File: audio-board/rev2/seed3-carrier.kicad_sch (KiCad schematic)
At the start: 55 parts, among them J1 AudioJack2_Switch, J2 AudioJack2, J3 POWER_BOARD, J4 DISPLAY_UART, J5 SJ3-35063AG, J8 LINE_OUT, J9 SJ3-35063AG, Q1 AO3401A, Q4 2N7002, U1 TLV9062IDR, U2 TPA6132A2RTE, U4 TXU0101

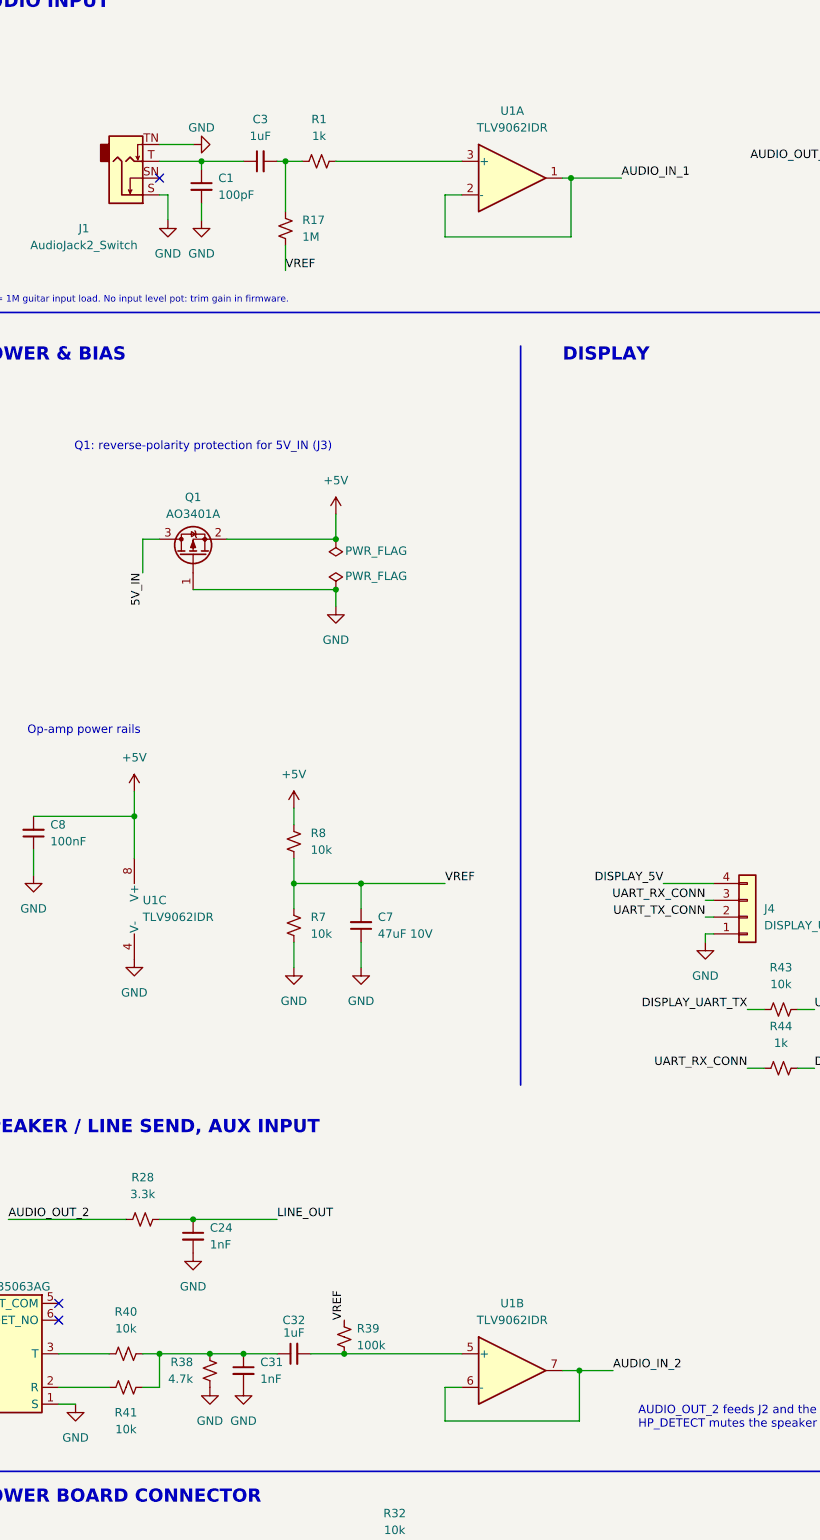
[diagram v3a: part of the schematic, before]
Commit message: Feed the AUX input straight to the Daisy and use a single op-amp
The Seed3's inputs are AC-coupled and the TAC5242 presents about 5k,
so the R40/R41 sum can drive Daisy pin 17 directly. This drops U1B,
C32 and R39, and R38 becomes a 100k DC return. U1 is now a TLV9061 in
SOT-23-5, with a two-unit project symbol, re-placed at the end of the
guitar row with C8 beside its V+ pin. TEST_PLAN 5.17 checks the AUX
level with the Daisy fitted.

Co-Authored-By: Claude Opus 5.5 <noreply@anthropic.com>
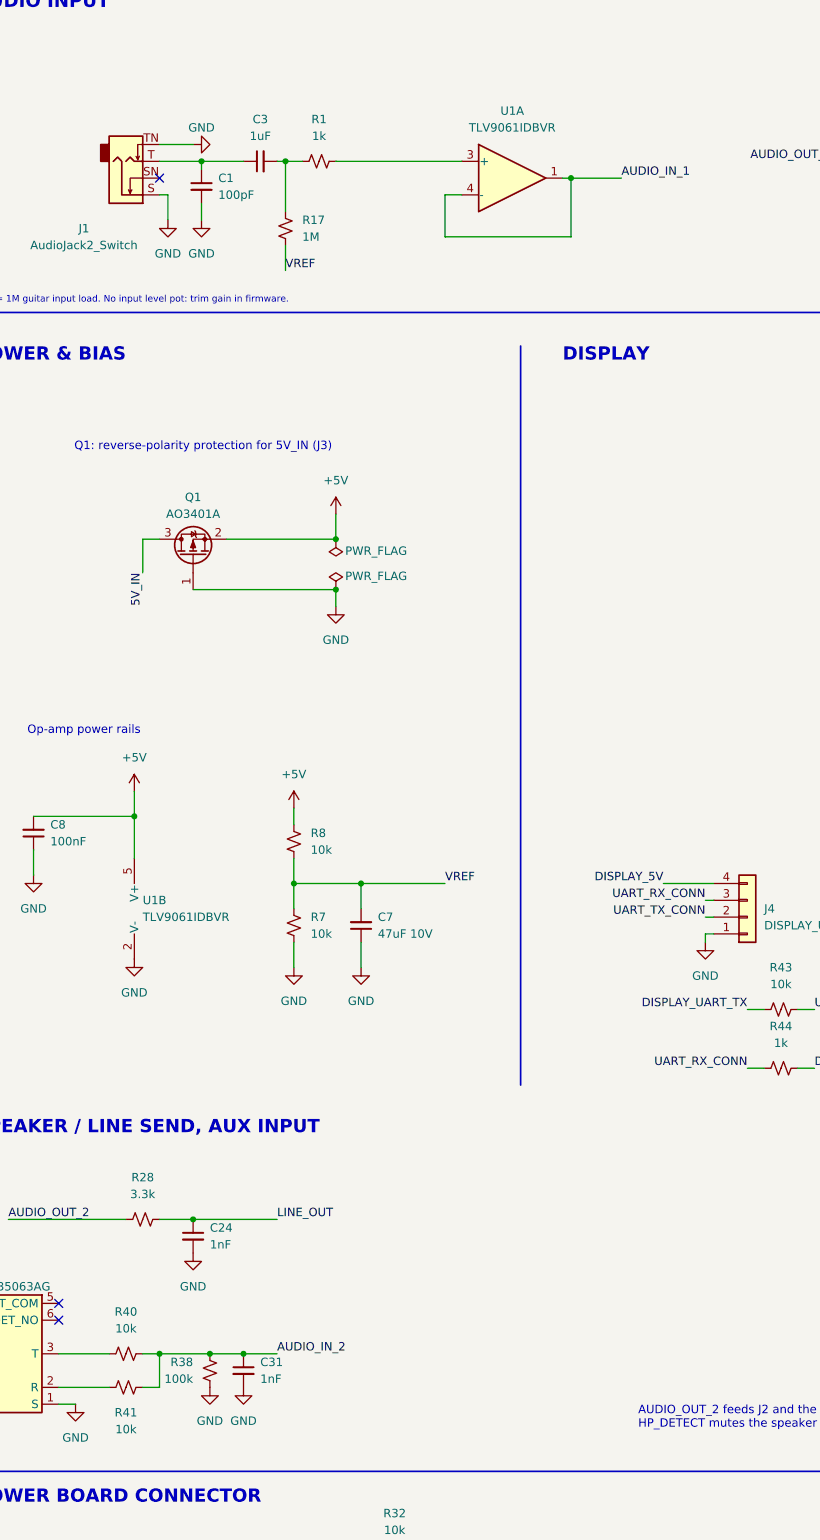
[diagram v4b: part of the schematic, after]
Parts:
- removed C32: 1uF, Capacitor_SMD:C_1206_3216Metric_Pad1.33x1.80mm_HandSolder, symbol Device:C_Small
- removed R39: 100k, Resistor_SMD:R_1206_3216Metric_Pad1.30x1.75mm_HandSolder, symbol Device:R_Small_US
- removed unit 2 of U1
- R38: value 4.7k -> 100k; LCSC C17936 -> C17900
- U1: value TLV9062IDR -> TLV9061IDBVR; footprint Package_SO:SOIC-8_3.9x4.9mm_P1.27mm -> Package_TO_SOT_SMD:SOT-23-5; symbol Amplifier_Operational:TL072 -> seed3-carrier:TLV9061DBV; LCSC C398355 -> C398358
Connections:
- net +5V: now also U1.5 (V+); no longer U1.8 (V+)
- net AUDIO_IN_1: now also U1.4 (-); no longer U1.2 (-)
- net AUDIO_IN_2: now also C31.1, R38.1, R40.2, R41.2
- net GND: now also U1.2 (V-); no longer U1.4 (V-)

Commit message: Remove U4, C37, C38 and R26 and tie U2 EN to +5V
The codec already powers down its DAC when an IWDG reset stops its
clocks, which silences the headphones as well as J2. Driving U2's EN
from the Daisy needed a level translator because the Daisy can run
from USB with +5V off, so drop it and leave U2 always on.

Co-Authored-By: Claude Opus 5.5 <noreply@anthropic.com>
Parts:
- removed C37, C38: 100nF, Capacitor_SMD:C_1206_3216Metric_Pad1.33x1.80mm_HandSolder, symbol Device:C_Small
- removed R26: 100k, Resistor_SMD:R_1206_3216Metric_Pad1.30x1.75mm_HandSolder, symbol Device:R_Small_US
- removed U4: TXU0101, Package_TO_SOT_SMD:SOT-23-6, symbol seed3-carrier:TXU0101DBV
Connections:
- net U2_EN is gone; now on net +5V: U2.13 (EN)
- net 3V3_D: no longer names the net of A1.38 (3V3_D)
- net HP_EN: no longer names the net of A1.33 (SAI2_SD_A)
- no-connect marks 27 -> 29
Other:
- note added: "U2 EN is tied to +5V: the headphone amp is on whenever +5V is up. A hung Daisy is muted by the codec, not by U2. The firmware feeds the STM32 internal watchdog (IWDG) only from the audio callback: if audio stops, the STM32 resets, its clocks stop, and the TAC5242 powers down its DAC (both outputs). Its pins float, and R37 holds SPK_EN low (Q4 off, speaker amp muted). The speaker amp mute is SPK_M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"
- note added: "U2: TPA6132A2 DirectPath, gain 0 dB (G0 high, G1 low). Outputs sit at 0 V: no output caps. C12/C13 with the 19.8k internal input R: 1.7 Hz high-pass. EN tied to +5V (always on). Layout: run SGND straight to the J5 sleeve pin. HPVDD/HPVSS are made inside U2: caps only."
- note removed: "HP_EN (Daisy pin 33) drives U2 EN through U4 (TXU0101, 3V3_D to +5V). U4 has a pull-down on A and goes Hi-Z when either supply is off, and R26 holds U2_EN low, so U2 stays off while the Daisy is absent, booting, in DFU, being reset, or running from USB with +5V off. The firmware feeds the STM32 internal watchdog (IWDG) only from the audio callback: if audio stops, the STM32 resets, its pins float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"
- note removed: "U2: TPA6132A2 DirectPath, gain 0 dB (G0 high, G1 low). Outputs sit at 0 V: no output caps. C12/C13 with the 19.8k internal input R: 1.7 Hz high-pass. EN = U2_EN from U4, pulled low by R26. Layout: run SGND straight to the J5 sleeve pin. HPVDD/HPVSS are made inside U2: caps only."

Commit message: Add a +5V sense on Daisy pin 22 to keep USB-only audio out of U2
With the Daisy on USB and +5V off, U2's charge pump rails sit at 0 V,
so its inputs are rated only to about +-0.3 V, while C12/C13 pass pin
18's full-scale +-1.4 V. R45/R46 (100k/100k) put +5V/2 on 5V_SENSE
(ADC_0) so the firmware can hold the outputs silent while +5V is down.

DESIGN.md sets the firmware thresholds and settle time and notes the
fast-power-loss limit; TEST_PLAN 5.18 scopes the transitions.

Co-Authored-By: Claude Opus 5.5 <noreply@anthropic.com>
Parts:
- added R45, R46: 100k, Resistor_SMD:R_1206_3216Metric_Pad1.30x1.75mm_HandSolder, symbol Device:R_Small_US
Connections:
- net +5V: now also R45.1
- net GND: now also R46.2
- net 5V_SENSE: now reaches A1.22 (ADC_0)
- net 5V_SENSE: now also R45.2, R46.1
- no-connect marks 29 -> 28

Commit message: Re-lay out the carrier schematic into framed functional sections
Group the sheet into eleven dashed, titled sections laid out left to
right (inputs and supply, Daisy and display, outputs, power board and
mute), moving each block rigidly so no connection changes. Misplaced
parts move to their own blocks: the AUX input, C17/C18, FB1/C30, J2/J8.

Rewrite every note in one style inside its section, correct the stale
HP_DETECT/SPK_EN note, and add notes for the AUX input, VREF, display
resistors and Daisy sockets. Update the title block, set J1/J2 to
NRJ4HF and C7/C18 to the 16 V parts on the BOM (board values match).

Co-Authored-By: Claude Opus 5.5 <noreply@anthropic.com>
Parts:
- C18, C7: value 47uF 10V -> 47uF 16V
- J1: value AudioJack2_Switch -> NRJ4HF
- J2: value AudioJack2 -> NRJ4HF
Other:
- note added: "A1 plugs into two 1×20 sockets. Unused pins are no-connect. USB stays on the module."
- note added: "AUDIO_OUT_2 drives J2 (external) and J8 (speaker amp) directly. R28/C24: ≈ 48 kHz low-pass. R4: DC return. With headphones in, the firmware drives SPK_EN low. J2 stays live."
- note added: "AUX INPUT"
- note added: "DAISY SEED3"
- note added: "GUITAR INPUT"
- note added: "HEADPHONE AMPLIFIER"
- note added: "HEADPHONE JACK & DETECT"
- note added: "J3 goes to the power board (JST-XH, 8 pins). Pins 5–7 are 3.3 V logic: nothing above 3.3 V on them. SPK_MUTE is open drain. The power board pulls it up, so the speaker amp stays muted unless SPK_EN is high. R32, R35 and R33 limit current into an unpowered Daisy. R34 holds PWR_HOLD low while the Daisy is absent or booting."
- note added: "J5 pins 5–6: isolated N/O switch, closes on plug insertion. HP_DETECT is LOW with headphones in. No external pull-up: the firmware enables PG9's internal pull-up. Bring-up: short TP11 to GND to simulate a plug."
- note added: "LINE OUT & SPEAKER SEND"
- note added: "MID-RAIL REFERENCE & OP-AMP SUPPLY"
- note added: "Mono to both channels, 16–64 Ω headphones. R2/C2: ≈ 64 kHz low-pass for DAC noise. U2: TPA6132A2 DirectPath, 0 dB inverting (G0 high, G1 low). Outputs sit at 0 V: no output caps. C12/C13 with U2's 19.8 kΩ inputs: 1.7 Hz high-pass. EN tied to +5V: always on. Layout: run SGND straight to the J5 sleeve. HPVDD/HPVSS are made inside U2: caps only."
- note added: "OUTPUT MUTE & +5V SENSE"
- note added: "POWER INPUT"
- note added: "Passive stereo-to-mono sum straight into AUDIO_IN_2. The Seed3 input is AC-coupled (≈ 5 kΩ): no buffer or coupling cap needed. R38 is the source's DC return. C31: RF filter (≈ 65 kHz)."
- note added: "Q1: reverse-polarity protection for 5V_IN (J3). C18 (low-ESR) damps the harness ringing. C17 is the entry ceramic."
- note added: "R17 (1 MΩ to VREF) sets the guitar load and the DC bias. U1A is a unity-gain buffer: input trim is in firmware. J1's tip switch shorts the input to GND with no plug in. C1 is an RF shunt. R1 protects U1A's input."
- note added: "R43/R44 limit current if the cable is miswired or hot-plugged. R43 is 10k so the Daisy's TX can't power an unpowered display (Daisy on USB): keep the UART at 230400 baud or less. FB1/C30 keep the display's current pulses (Wi-Fi, backlight) off +5V."
- note added: "U2 EN is tied to +5V. A hung Daisy is muted by the codec: the firmware feeds the STM32 IWDG only from the audio callback, so if audio stops the STM32 resets, its clocks stop and the TAC5242 powers down its DAC. R37 holds SPK_EN low (speaker muted) during a reset. 5V_SENSE ≈ 2.5 V when +5V is up. With +5V off (Daisy on USB) the firmware keeps both outputs silent: U2's inputs are rated only to its 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"
- note added: "VREF ≈ 2.5 V, only load R17. C7 keeps +5V noise from the display out of VREF (≈ 0.7 Hz). C8 decouples U1 at pin 5."
- note removed: "AUDIO INPUT"
- note removed: "AUDIO_OUT_2 feeds J2 and the speaker amp (J8) directly. HP_DETECT mutes the speaker amp (SPK_EN); J2 stays live."
- note removed: "DAISY SEED"
- note removed: "HEADPHONE FILTER"
- note removed: "HEADPHONE OUTPUT"
- note removed: "Headphone detect: J5 pins 5-6 are an isolated N-O switch that closes on plug insertion, so HP_DETECT is LOW with headphones in. No external pull-up: the firmware enables PG9's internal pull-up, so the line floats until it runs. Bring-up: short TP11 to GND to simulate it."
- note removed: "J3 goes to the power board (JST-XH, 8 pins). Pins 5-7 are 3.3 V logic: nothing above 3.3 V on them. SPK_MUTE is open drain. The power board pulls it up, so the speaker amp stays muted unless SPK_EN is high."
- note removed: "Mono to both ears / 16-64 ohm headphones"
- note removed: "OUTPUT MUTE"
- note removed: "Op-amp power rails"
- note removed: "POWER & BIAS"
- note removed: "Q1: reverse-polarity protection for 5V_IN (J3)"
- note removed: "R17 = 1M guitar input load. No input level pot: trim gain in firmware."
- note removed: "SPEAKER / LINE SEND, AUX INPUT"
- note removed: "U2 EN is tied to +5V: the headphone amp is on whenever +5V is up. A hung Daisy is muted by the codec, not by U2. The firmware feeds the STM32 internal watchdog (IWDG) only from the audio callback: if audio stops, the STM32 resets, its clocks stop, and the TAC5242 powers down its DAC (both outputs). Its pins float, and R37 holds SPK_EN low (Q4 off, speaker amp muted). The speaker amp mute is SPK_M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"
- note removed: "U2: TPA6132A2 DirectPath, gain 0 dB (G0 high, G1 low). Outputs sit at 0 V: no output caps. C12/C13 with the 19.8k internal input R: 1.7 Hz high-pass. EN tied to +5V (always on). Layout: run SGND straight to the J5 sleeve pin. HPVDD/HPVSS are made inside U2: caps only."
- moved on the sheet: A1, C1, C12, C13, C17, C18, C2, C24, C28, C29, C3, C30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

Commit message: Re-annotate the carrier board in sheet order
Renumber R, C, J, Q and TP left to right, then top to bottom by
section, so the designators have no gaps: R1-R19, C1-C18, J1-J7,
Q1-Q2, TP1. U1, U2, A1 and FB1 keep their numbers, so the U1/U2
design rules are unchanged.

Apply one mapping to the schematic, the board, the sheet notes and
DESIGN.md/TEST_PLAN.md, and rename the five auto-generated board nets
that embed a designator. CHANGES.md names removed parts by their rev 1
designator and lists every old number against its new one.

Netlists before and after match net for net once the old one is
translated through the mapping; ERC and schematic parity are clean.

Co-Authored-By: Claude Opus 5.5 <noreply@anthropic.com>
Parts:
- renumbered C12 to C10, C13 to C11, C33 to C12, C35 to C13, C36 to C14, C34 to C15, C24 to C16, C28 to C17, C29 to C18, C3 to C2, C31 to C3, C17 to C4, C18 to C5, C8 to C6, C30 to C8, C2 to C9, J9 to J2, J4 to J3, J5 to J4, J2 to J5, J8 to J6, J3 to J7, Q4 to Q2, R17 to R1, R2 to R10, R28 to R11, R4 to R12, R32 to R13, R33 to R14, R34 to R15, R35 to R16, R37 to R17, R45 to R18, R46 to R19, R1 to R2, R40 to R3, R41 to R4, R38 to R5, R8 to R6, R43 to R8, R44 to R9, TP11 to TP1
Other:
- note added: "AUDIO_OUT_2 drives J5 (external) and J6 (speaker amp) directly. R11/C16: ≈ 48 kHz low-pass. R12: DC return. With headphones in, the firmware drives SPK_EN low. J5 stays live."
- note added: "J4 pins 5–6: isolated N/O switch, closes on plug insertion. HP_DETECT is LOW with headphones in. No external pull-up: the firmware enables PG9's internal pull-up. Bring-up: short TP1 to GND to simulate a plug."
- note added: "J7 goes to the power board (JST-XH, 8 pins). Pins 5–7 are 3.3 V logic: nothing above 3.3 V on them. SPK_MUTE is open drain. The power board pulls it up, so the speaker amp stays muted unless SPK_EN is high. R13, R16 and R14 limit current into an unpowered Daisy. R15 holds PWR_HOLD low while the Daisy is absent or booting."
- note added: "Mono to both channels, 16–64 Ω headphones. R10/C9: ≈ 64 kHz low-pass for DAC noise. U2: TPA6132A2 DirectPath, 0 dB inverting (G0 high, G1 low). Outputs sit at 0 V: no output caps. C10/C11 with U2's 19.8 kΩ inputs: 1.7 Hz high-pass. EN tied to +5V: always on. Layout: run SGND straight to the J4 sleeve. HPVDD/HPVSS are made inside U2: caps only."
- note added: "Passive stereo-to-mono sum straight into AUDIO_IN_2. The Seed3 input is AC-coupled (≈ 5 kΩ): no buffer or coupling cap needed. R5 is the source's DC return. C3: RF filter (≈ 65 kHz)."
- note added: "Q1: reverse-polarity protection for 5V_IN (J7). C5 (low-ESR) damps the harness ringing. C4 is the entry ceramic."
- note added: "R1 (1 MΩ to VREF) sets the guitar load and the DC bias. U1A is a unity-gain buffer: input trim is in firmware. J1's tip switch shorts the input to GND with no plug in. C1 is an RF shunt. R2 protects U1A's input."
- note added: "R8/R9 limit current if the cable is miswired or hot-plugged. R8 is 10k so the Daisy's TX can't power an unpowered display (Daisy on USB): keep the UART at 230400 baud or less. FB1/C8 keep the display's current pulses (Wi-Fi, backlight) off +5V."
- note added: "U2 EN is tied to +5V. A hung Daisy is muted by the codec: the firmware feeds the STM32 IWDG only from the audio callback, so if audio stops the STM32 resets, its clocks stop and the TAC5242 powers down its DAC. R17 holds SPK_EN low (speaker muted) during a reset. 5V_SENSE ≈ 2.5 V when +5V is up. With +5V off (Daisy on USB) the firmware keeps both outputs silent: U2's inputs are rated only to its 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"
- note added: "VREF ≈ 2.5 V, only load R1. C7 keeps +5V noise from the display out of VREF (≈ 0.7 Hz). C6 decouples U1 at pin 5."
- note removed: "AUDIO_OUT_2 drives J2 (external) and J8 (speaker amp) directly. R28/C24: ≈ 48 kHz low-pass. R4: DC return. With headphones in, the firmware drives SPK_EN low. J2 stays live."
- note removed: "J3 goes to the power board (JST-XH, 8 pins). Pins 5–7 are 3.3 V logic: nothing above 3.3 V on them. SPK_MUTE is open drain. The power board pulls it up, so the speaker amp stays muted unless SPK_EN is high. R32, R35 and R33 limit current into an unpowered Daisy. R34 holds PWR_HOLD low while the Daisy is absent or booting."
- note removed: "J5 pins 5–6: isolated N/O switch, closes on plug insertion. HP_DETECT is LOW with headphones in. No external pull-up: the firmware enables PG9's internal pull-up. Bring-up: short TP11 to GND to simulate a plug."
- note removed: "Mono to both channels, 16–64 Ω headphones. R2/C2: ≈ 64 kHz low-pass for DAC noise. U2: TPA6132A2 DirectPath, 0 dB inverting (G0 high, G1 low). Outputs sit at 0 V: no output caps. C12/C13 with U2's 19.8 kΩ inputs: 1.7 Hz high-pass. EN tied to +5V: always on. Layout: run SGND straight to the J5 sleeve. HPVDD/HPVSS are made inside U2: caps only."
- note removed: "Passive stereo-to-mono sum straight into AUDIO_IN_2. The Seed3 input is AC-coupled (≈ 5 kΩ): no buffer or coupling cap needed. R38 is the source's DC return. C31: RF filter (≈ 65 kHz)."
- note removed: "Q1: reverse-polarity protection for 5V_IN (J3). C18 (low-ESR) damps the harness ringing. C17 is the entry ceramic."
- note removed: "R17 (1 MΩ to VREF) sets the guitar load and the DC bias. U1A is a unity-gain buffer: input trim is in firmware. J1's tip switch shorts the input to GND with no plug in. C1 is an RF shunt. R1 protects U1A's input."
- note removed: "R43/R44 limit current if the cable is miswired or hot-plugged. R43 is 10k so the Daisy's TX can't power an unpowered display (Daisy on USB): keep the UART at 230400 baud or less. FB1/C30 keep the display's current pulses (Wi-Fi, backlight) off +5V."
- note removed: "U2 EN is tied to +5V. A hung Daisy is muted by the codec: the firmware feeds the STM32 IWDG only from the audio callback, so if audio stops the STM32 resets, its clocks stop and the TAC5242 powers down its DAC. R37 holds SPK_EN low (speaker muted) during a reset. 5V_SENSE ≈ 2.5 V when +5V is up. With +5V off (Daisy on USB) the firmware keeps both outputs silent: U2's inputs are rated only to its 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"
- note removed: "VREF ≈ 2.5 V, only load R17. C7 keeps +5V noise from the display out of VREF (≈ 0.7 Hz). C8 decouples U1 at pin 5."
